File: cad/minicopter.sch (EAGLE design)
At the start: 37 parts, among them CN2 DO NOT PLACE, U1 STM32F411/48, U2 LSM6DS3, U3 DRV8835, U4 LPS25HB

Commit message: motor driver
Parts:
- removed U$2, U$3: FIDUCIAL, jaw:FIDUCIAL
- added U5: DRV8839, jaw:DRV8839
- U3: value DRV8835 -> DRV8839; device jaw:DRV8835 -> jaw:DRV8839
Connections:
- net GND: now also U5.GND; no longer U3.MODE
- net IOA0: now also U5.IN1; no longer U3.APH
- net IOA1: now also U5.IN2; no longer U3.AEN
- net IOA2: now also U3.IN1; no longer U3.BPH
- net IOA3: now also U3.IN2; no longer U3.BEN
- net N$16: now also U5.OUT1; no longer U3.A1
- net N$17: now also U5.OUT2; no longer U3.A2
- net N$19: now also U3.OUT1; no longer U3.B1
- net N$20: now also U3.OUT2; no longer U3.B2
- net VCC: now also U3.EN1, U3.EN2, U3.NSLEEP, U5.EN1, U5.EN2, U5.NSLEEP, U5.VCC
- net VCCM: now also U5.VM

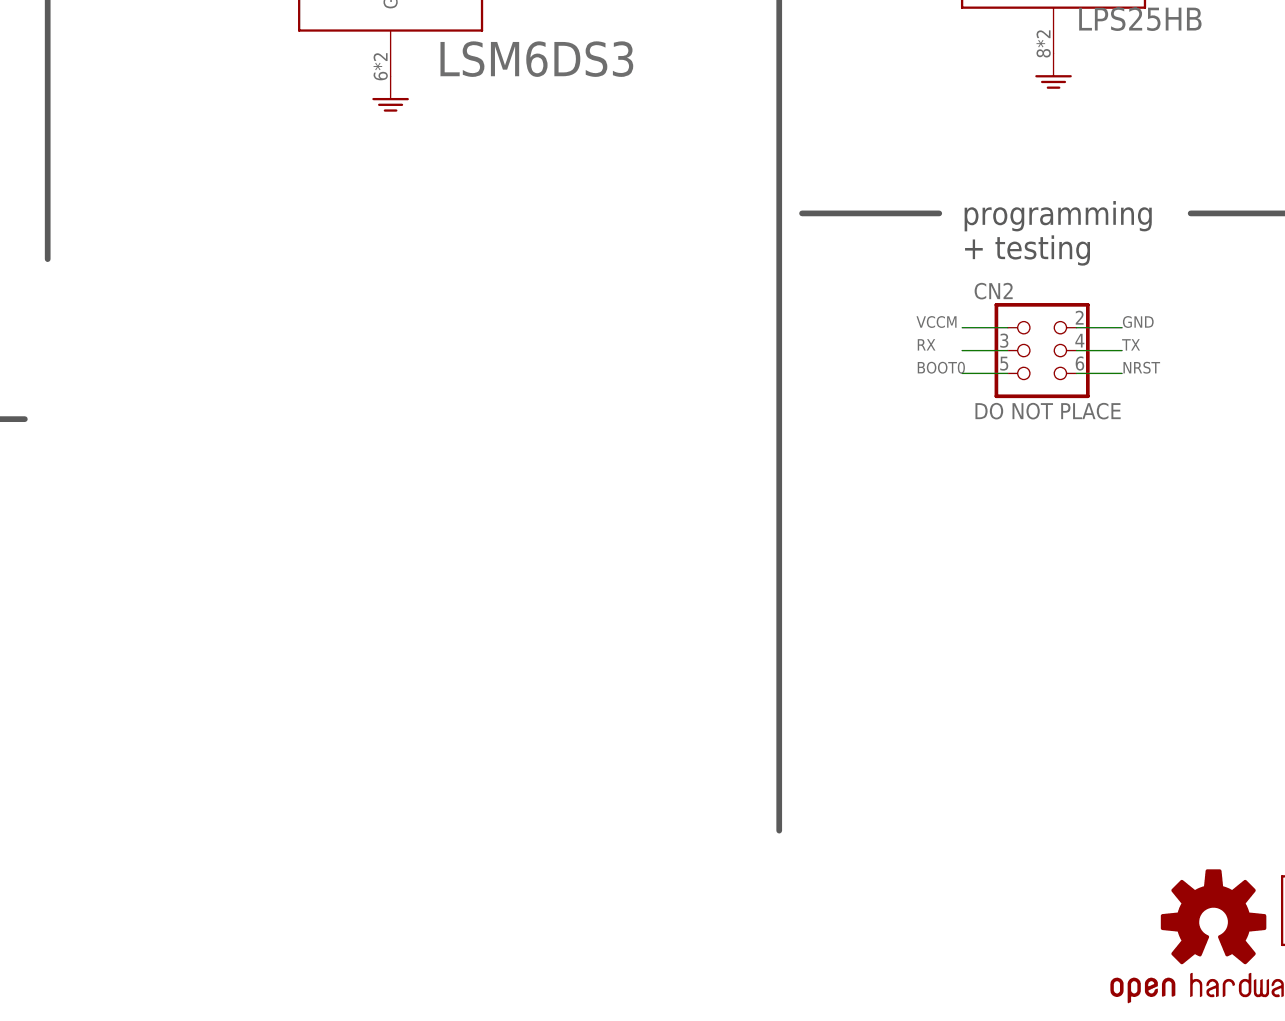
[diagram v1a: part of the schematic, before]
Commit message: add magnetometer
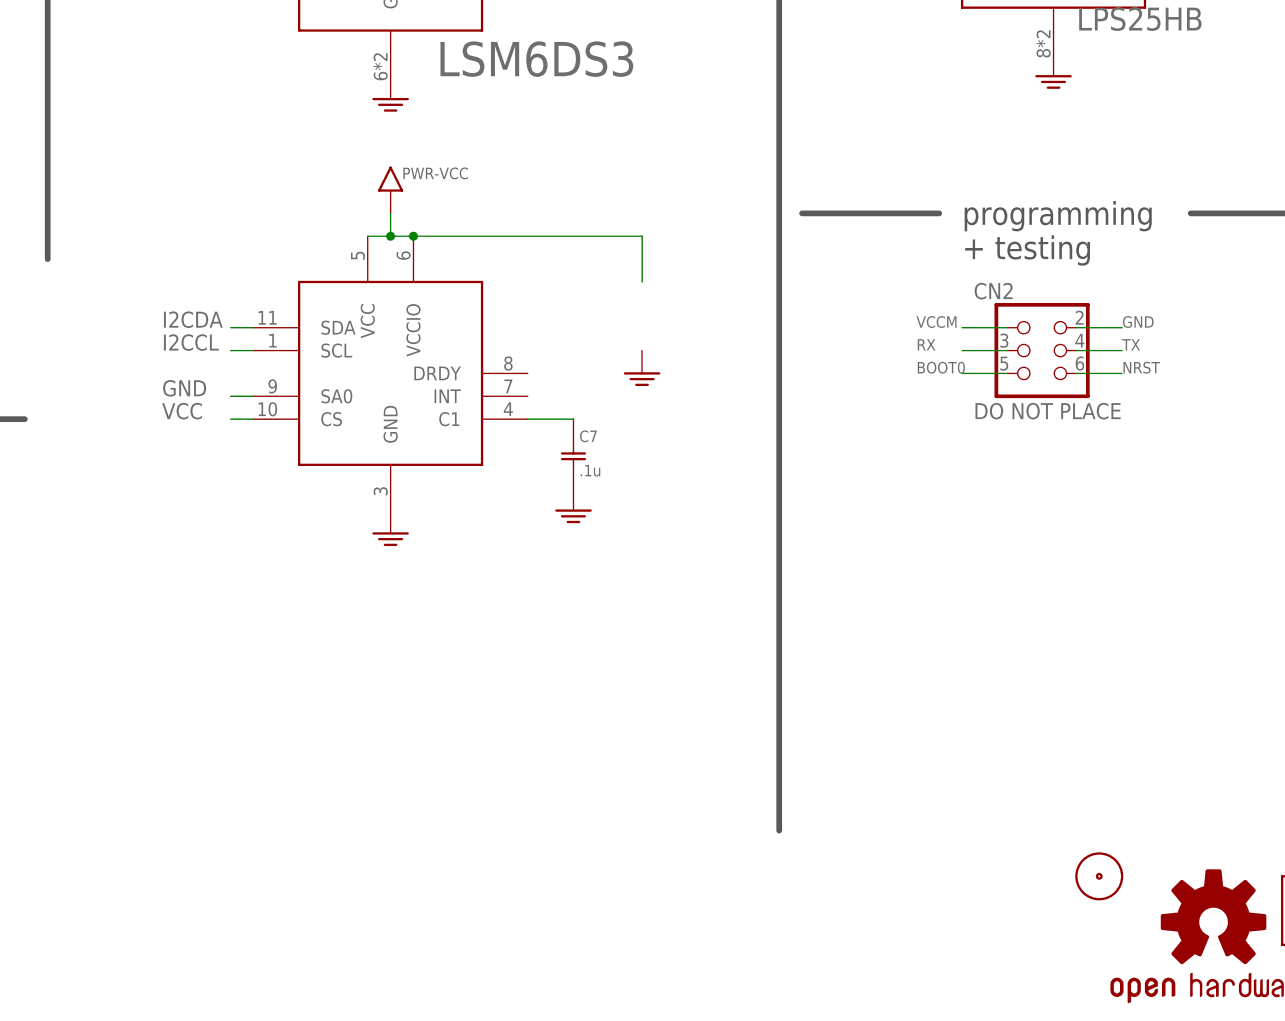
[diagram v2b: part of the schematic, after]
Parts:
- added C7: .1u, jaw:C0603
- added U$2: FIDUCIAL, jaw:FIDUCIAL
- added U6: LIS3MDL, jaw:LIS3MDL
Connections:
- new net N$23: C7.P$1, U6.C1
- net GND: now also C7.P$2, U6.GND, U6.SA0
- net I2CCL: now also U6.SCL
- net I2CDA: now also U6.SDA
- net VCC: now also U6.CS, U6.VCC, U6.VCCIO
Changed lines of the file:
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@@
 <part name="VCCM5" library="jaw" deviceset="PWR-VCCM" device=""/>
 <part name="GND17" library="jaw" deviceset="PWR-GND" device=""/>
+<part name="U6" library="jaw" deviceset="LIS3MDL" device=""/>
+<part name="C7" library="jaw" deviceset="C" device="0603" value=".1u"/>
+<part name="GND19" library="jaw" deviceset="PWR-GND" device=""/>
+<part name="VCC12" library="jaw" deviceset="PWR-VCC" device=""/>
+<part name="GND21" library="jaw" deviceset="PWR-GND" device=""/>
+<part name="GND22" library="jaw" deviceset="PWR-GND" device=""/>
+<part name="U$2" library="jaw" deviceset="FIDUCIAL" device=""/>
 </parts>
 <sheets>
@@
 <instance part="VCCM5" gate="G$1" x="307.34" y="210.82"/>
 <instance part="GND17" gate="G$1" x="309.88" y="172.72"/>
+<instance part="U6" gate="G$1" x="314.96" y="88.9"/>
+<instance part="C7" gate="G$1" x="335.28" y="78.74"/>
+<instance part="GND19" gate="G$1" x="314.96" y="71.12"/>
+<instance part="VCC12" gate="G$1" x="314.96" y="109.22"/>
+<instance part="GND21" gate="G$1" x="335.28" y="73.66"/>
+<instance part="GND22" gate="G$1" x="342.9" y="88.9"/>
+<instance part="U$2" gate="G$1" x="393.7" y="33.02"/>
 </instances>
 <busses>
@@
 <pinref part="GND17" gate="G$1" pin="GND"/>
 </segment>
+<segment>
+<pinref part="U6" gate="G$1" pin="GND"/>
+<pinref part="GND19" gate="G$1" pin="GND"/>
+</segment>
+<segment>
+<pinref part="U6" gate="G$1" pin="SA0"/>
+<wire x1="299.72" y1="86.36" x2="297.18" y2="86.36" width="0.1524" layer="91"/>
+<label x="289.56" y="86.36" size="1.778" layer="95" ratio="10"/>
+</segment>
+<segment>
+<pinref part="C7" gate="G$1" pin="P$2"/>
+<pinref part="GND21" gate="G$1" pin="GND"/>
+</segment>
 </net>
 <net name="VCC" class="0">
@@
 <label x="287.02" y="185.42" size="1.778" layer="95" ratio="10"/>
 </segment>
+<segment>
+<pinref part="U6" gate="G$1" pin="VCC"/>
+<pinref part="U6" gate="G$1" pin="VCCIO"/>
+<wire x1="312.42" y1="104.14" x2="314.96" y2="104.14" width="0.1524" layer="91"/>
+<pinref part="VCC12" gate="G$1" pin="VCC"/>
+<wire x1="314.96" y1="104.14" x2="317.5" y2="104.14" width="0.1524" layer="91"/>
+<wire x1="314.96" y1="106.68" x2="314.96" y2="104.14" width="0.1524" layer="91"/>
+<junction x="314.96" y="104.14"/>
+<wire x1="317.5" y1="104.14" x2="342.9" y2="104.14" width="0.1524" layer="91"/>
+<wire x1="342.9" y1="104.14" x2="342.9" y2="99.06" width="0.1524" layer="91"/>
+<junction x="317.5" y="104.14"/>
+</segment>
+<segment>
+<pinref part="U6" gate="G$1" pin="CS"/>
+<wire x1="299.72" y1="83.82" x2="297.18" y2="83.82" width="0.1524" layer="91"/>
+<label x="289.56" y="83.82" size="1.778" layer="95" ratio="10"/>
+</segment>
 </net>
 <net name="BOOT0" class="0">
@@
 <label x="363.22" y="142.24" size="1.778" layer="95" ratio="10"/>
 </segment>
+<segment>
+<pinref part="U6" gate="G$1" pin="SCL"/>
+<wire x1="299.72" y1="91.44" x2="297.18" y2="91.44" width="0.1524" layer="91"/>
+<label x="289.56" y="91.44" size="1.778" layer="95" ratio="10"/>
+</segment>
 </net>
 <net name="I2CDA" class="0">
@@
 <wire x1="373.38" y1="139.7" x2="370.84" y2="139.7" width="0.1524" layer="91"/>
 <label x="363.22" y="139.7" size="1.778" layer="95" ratio="10"/>
+</segment>
+<segment>
+<pinref part="U6" gate="G$1" pin="SDA"/>
+<wire x1="299.72" y1="93.98" x2="297.18" y2="93.98" width="0.1524" layer="91"/>
+<label x="289.56" y="93.98" size="1.778" layer="95" ratio="10"/>
 </segment>
 </net>
@@
 </segment>
 </net>
+<net name="N$23" class="0">
+<segment>
+<pinref part="U6" gate="G$1" pin="C1"/>
+<pinref part="C7" gate="G$1" pin="P$1"/>
+<wire x1="330.2" y1="83.82" x2="335.28" y2="83.82" width="0.1524" layer="91"/>
+</segment>
+</net>

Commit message: tweak
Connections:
- net GND: now also CN1.P$2, CN1.P$6; no longer CN1.P$1, CN1.P$5
- net N$16: now also CN1.P$1; no longer CN1.P$2
- net N$19: now also CN1.P$5; no longer CN1.P$6
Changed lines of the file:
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@@
 <instance part="VCCM3" gate="G$1" x="307.34" y="259.08"/>
 <instance part="GND9" gate="G$1" x="309.88" y="220.98"/>
-<instance part="GND10" gate="G$1" x="373.38" y="193.04"/>
+<instance part="GND10" gate="G$1" x="378.46" y="182.88"/>
 <instance part="VCC5" gate="G$1" x="231.14" y="200.66"/>
 <instance part="VCC6" gate="G$1" x="210.82" y="172.72"/>
@@
 </segment>
 <segment>
-<pinref part="CN1" gate="A" pin="P$1"/>
-<wire x1="368.3" y1="208.28" x2="373.38" y2="208.28" width="0.1524" layer="91"/>
-<wire x1="373.38" y1="208.28" x2="373.38" y2="205.74" width="0.1524" layer="91"/>
 <pinref part="CN1" gate="A" pin="P$3"/>
-<wire x1="373.38" y1="205.74" x2="373.38" y2="203.2" width="0.1524" layer="91"/>
-<wire x1="373.38" y1="203.2" x2="373.38" y2="200.66" width="0.1524" layer="91"/>
-<wire x1="373.38" y1="200.66" x2="373.38" y2="195.58" width="0.1524" layer="91"/>
-<wire x1="368.3" y1="205.74" x2="373.38" y2="205.74" width="0.1524" layer="91"/>
-<junction x="373.38" y="205.74"/>
-<pinref part="CN1" gate="A" pin="P$5"/>
-<wire x1="368.3" y1="203.2" x2="373.38" y2="203.2" width="0.1524" layer="91"/>
-<junction x="373.38" y="203.2"/>
+<wire x1="378.46" y1="205.74" x2="378.46" y2="203.2" width="0.1524" layer="91"/>
+<wire x1="378.46" y1="203.2" x2="378.46" y2="200.66" width="0.1524" layer="91"/>
+<wire x1="378.46" y1="200.66" x2="378.46" y2="187.96" width="0.1524" layer="91"/>
+<wire x1="378.46" y1="187.96" x2="378.46" y2="185.42" width="0.1524" layer="91"/>
+<wire x1="368.3" y1="205.74" x2="378.46" y2="205.74" width="0.1524" layer="91"/>
 <pinref part="CN1" gate="A" pin="P$7"/>
-<wire x1="368.3" y1="200.66" x2="373.38" y2="200.66" width="0.1524" layer="91"/>
-<junction x="373.38" y="200.66"/>
+<wire x1="368.3" y1="200.66" x2="378.46" y2="200.66" width="0.1524" layer="91"/>
+<junction x="378.46" y="200.66"/>
 <pinref part="GND10" gate="G$1" pin="GND"/>
+<pinref part="CN1" gate="A" pin="P$2"/>
+<wire x1="360.68" y1="208.28" x2="353.06" y2="208.28" width="0.1524" layer="91"/>
+<wire x1="353.06" y1="208.28" x2="353.06" y2="203.2" width="0.1524" layer="91"/>
+<pinref part="CN1" gate="A" pin="P$6"/>
+<wire x1="353.06" y1="203.2" x2="360.68" y2="203.2" width="0.1524" layer="91"/>
+<wire x1="353.06" y1="203.2" x2="353.06" y2="187.96" width="0.1524" layer="91"/>
+<junction x="353.06" y="203.2"/>
+<wire x1="353.06" y1="187.96" x2="378.46" y2="187.96" width="0.1524" layer="91"/>
+<junction x="378.46" y="187.96"/>
 </segment>
 <segment>
@@
 <net name="N$16" class="0">
 <segment>
-<pinref part="CN1" gate="A" pin="P$2"/>
-<wire x1="342.9" y1="208.28" x2="360.68" y2="208.28" width="0.1524" layer="91"/>
 <pinref part="U5" gate="G$1" pin="OUT1"/>
 <wire x1="325.12" y1="241.3" x2="342.9" y2="241.3" width="0.1524" layer="91"/>
-<wire x1="342.9" y1="241.3" x2="342.9" y2="208.28" width="0.1524" layer="91"/>
+<wire x1="342.9" y1="241.3" x2="373.38" y2="241.3" width="0.1524" layer="91"/>
+<wire x1="373.38" y1="241.3" x2="373.38" y2="208.28" width="0.1524" layer="91"/>
+<pinref part="CN1" gate="A" pin="P$1"/>
+<wire x1="373.38" y1="208.28" x2="368.3" y2="208.28" width="0.1524" layer="91"/>
 </segment>
 </net>
@@
 <net name="N$19" class="0">
 <segment>
-<pinref part="CN1" gate="A" pin="P$6"/>
-<wire x1="345.44" y1="203.2" x2="360.68" y2="203.2" width="0.1524" layer="91"/>
 <pinref part="U3" gate="G$1" pin="OUT1"/>
 <wire x1="325.12" y1="193.04" x2="340.36" y2="193.04" width="0.1524" layer="91"/>
-<wire x1="340.36" y1="193.04" x2="340.36" y2="203.2" width="0.1524" layer="91"/>
-<wire x1="340.36" y1="203.2" x2="345.44" y2="203.2" width="0.1524" layer="91"/>
-</segment>
-</net>
+<wire x1="340.36" y1="193.04" x2="373.38" y2="193.04" width="0.1524" layer="91"/>
+<wire x1="373.38" y1="193.04" x2="373.38" y2="203.2" width="0.1524" layer="91"/>
+<pinref part="CN1" gate="A" pin="P$5"/>
+<wire x1="373.38" y1="203.2" x2="368.3" y2="203.2" width="0.1524" layer="91"/>
+</segment>
+</net>
